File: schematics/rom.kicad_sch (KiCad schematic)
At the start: 8 parts, among them J3 XLR3_Switched, J4 XLR3_Switched, J5 myBus, U4 71256SA, U5 4NAND

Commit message: Fix errors in schematics
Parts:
- removed J3, J4: XLR3_Switched, symbol Connector:XLR3_Switched
- added SW2, SW3: SW_SPDT, symbol Switch:SW_SPDT
- renumbered J5 to J3
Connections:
- net +5V: now also SW2.3 (C), SW3.3 (C)
- net GND: now also SW2.1 (A), SW3.1 (A)
- net Prog: now also SW2.2 (B)
- net at U4.1 (A14): now also SW3.2 (B)
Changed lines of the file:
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@@
 	(wire
 		(pts
-			(xy 45.72 96.52) (xy 41.91 96.52)
+			(xy 41.91 96.52) (xy 48.26 96.52)
 		)
 		(stroke
@@
 	(wire
 		(pts
+			(xy 71.12 68.58) (xy 82.55 68.58)
+		)
+		(stroke
+			(width 0)
+			(type default)
+		)
+	)
+	(wire
+		(pts
 			(xy 82.55 96.52) (xy 77.47 96.52)
 		)
@@
 	(wire
 		(pts
+			(xy 58.42 93.98) (xy 60.96 93.98)
+		)
+		(stroke
+			(width 0)
+			(type default)
+		)
+	)
+	(wire
+		(pts
 			(xy 156.21 83.82) (xy 156.21 88.9)
 		)
@@
 	(wire
 		(pts
-			(xy 41.91 91.44) (xy 45.72 91.44)
+			(xy 41.91 91.44) (xy 48.26 91.44)
 		)
 		(stroke
@@
 	(wire
 		(pts
-			(xy 54.61 66.04) (xy 58.42 66.04)
+			(xy 54.61 66.04) (xy 60.96 66.04)
 		)
 		(stroke
@@
 	(wire
 		(pts
-			(xy 58.42 71.12) (xy 54.61 71.12)
-		)
-		(stroke
-			(width 0)
-			(type default)
-		)
-	)
-	(wire
-		(pts
-			(xy 82.55 68.58) (xy 73.66 68.58)
+			(xy 54.61 71.12) (xy 60.96 71.12)
 		)
 		(stroke
@@
 		)
 	)
+	(label "D[0..7]"
+		(at 138.43 129.54 90)
+		(fields_autoplaced yes)
+		(effects
+			(font
+				(size 1.27 1.27)
+				(bold yes)
+			)
+			(justify left bottom)
+		)
+	)
 	(label "D6"
 		(at 106.68 93.98 0)
@@
 		)
 	)
+	(label "A[0..15]"
+		(at 115.57 132.08 90)
+		(fields_autoplaced yes)
+		(effects
+			(font
+				(size 1.27 1.27)
+				(bold yes)
+			)
+			(justify left bottom)
+		)
+	)
 	(label "D0"
 		(at 120.65 142.24 90)
@@
 			)
 			(justify left bottom)
+		)
+	)
+	(symbol
+		(lib_id "Switch:SW_SPDT")
+		(at 66.04 68.58 180)
+		(unit 1)
+		(exclude_from_sim no)
+		(in_bom yes)
+		(on_board yes)
+		(dnp no)
+		(fields_autoplaced yes)
+		(property "Reference" "SW3"
+			(at 66.04 59.69 0)
+			(effects
+				(font
+					(size 1.27 1.27)
+				)
+			)
+		)
+		(property "Value" "SW_SPDT"
+			(at 66.04 62.23 0)
+			(effects
+				(font
+					(size 1.27 1.27)
+				)
+			)
+		)
+		(property "Footprint" ""
+			(at 66.04 68.58 0)
+			(effects
+				(font
+					(size 1.27 1.27)
+				)
+				(hide yes)
+			)
+		)
+		(property "Datasheet" "~"
+			(at 66.04 60.96 0)
+			(effects
+				(font
+					(size 1.27 1.27)
+				)
+				(hide yes)
+			)
+		)
+		(property "Description" "Switch, single pole double throw"
+			(at 66.04 68.58 0)
+			(effects
+				(font
+					(size 1.27 1.27)
+				)
+				(hide yes)
+			)
+		)
+		(pin "1"
+		)
+		(pin "3"
+		)
+		(pin "2"
+		)
+		(instances
+			(project "markus"
+				(path "/03a78ca6-eaff-4f05-be7b-36cd15f8b56d/4e0565c2-54d5-42cd-9fad-4b6deda009d9"
+					(reference "SW3")
+					(unit 1)
+				)
+			)
 		)
 	)
@@
 	)
 	(symbol
+		(lib_id "Switch:SW_SPDT")
+		(at 53.34 93.98 180)
+		(unit 1)
+		(exclude_from_sim no)
+		(in_bom yes)
+		(on_board yes)
+		(dnp no)
+		(fields_autoplaced yes)
+		(property "Reference" "SW2"
+			(at 53.34 85.09 0)
+			(effects
+				(font
+					(size 1.27 1.27)
+				)
+			)
+		)
+		(property "Value" "SW_SPDT"
+			(at 53.34 87.63 0)
+			(effects
+				(font
+					(size 1.27 1.27)
+				)
+			)
+		)
+		(property "Footprint" ""
+			(at 53.34 93.98 0)
+			(effects
+				(font
+					(size 1.27 1.27)
+				)
+				(hide yes)
+			)
+		)
+		(property "Datasheet" "~"
+			(at 53.34 86.36 0)
+			(effects
+				(font
+					(size 1.27 1.27)
+				)
+				(hide yes)
+			)
+		)
+		(property "Description" "Switch, single pole double throw"
+			(at 53.34 93.98 0)
+			(effects
+				(font
+					(size 1.27 1.27)
+				)
+				(hide yes)
+			)
+		)
+		(pin "1"
+		)
+		(pin "3"
+		)
+		(pin "2"
+		)
+		(instances
+			(project ""
+				(path "/03a78ca6-eaff-4f05-be7b-36cd15f8b56d/4e0565c2-54d5-42cd-9fad-4b6deda009d9"
+					(reference "SW2")
+					(unit 1)
+				)
+			)
+		)
+	)
+	(symbol
 		(lib_id "power:+5V")
 		(at 48.26 135.89 0)
@@
 	)
 	(symbol
-		(lib_id "Connector:XLR3_Switched")
-		(at 66.04 68.58 180)
-		(unit 2)
-		(exclude_from_sim no)
-		(in_bom yes)
-		(on_board yes)
-		(dnp no)
-		(property "Reference" "J4"
-			(at 66.04 59.2582 0)
-			(effects
-				(font
-					(size 1.27 1.27)
-				)
-			)
-		)
-		(property "Value" "XLR3_Switched"
-			(at 66.04 61.5696 0)
-			(effects
-				(font
-					(size 1.27 1.27)
-				)
-			)
-		)
-		(property "Footprint" ""
-			(at 66.04 71.12 0)
-			(effects
-				(font
-					(size 1.27 1.27)
-				)
-				(hide yes)
-			)
-		)
-		(property "Datasheet" " ~"
-			(at 66.04 71.12 0)
-			(effects
-				(font
-					(size 1.27 1.27)
-				)
-				(hide yes)
-			)
-		)
-		(property "Description" ""
-			(at 66.04 68.58 0)
-			(effects
-				(font
-					(size 1.27 1.27)
-				)
-				(hide yes)
-			)
-		)
-		(pin "3"
-		)
-		(pin "1"
-		)
-		(pin "2"
-		)
-		(pin "NO"
-		)
-		(pin "N"
-		)
-		(pin "NC"
-		)
-		(instances
-			(project "markus"
-				(path "/03a78ca6-eaff-4f05-be7b-36cd15f8b56d/4e0565c2-54d5-42cd-9fad-4b6deda009d9"
-					(reference "J4")
-					(unit 2)
-				)
-			)
-		)
-	)
-	(symbol
-		(lib_id "Connector:XLR3_Switched")
-		(at 53.34 93.98 180)
-		(unit 2)
-		(exclude_from_sim no)
-		(in_bom yes)
-		(on_board yes)
-		(dnp no)
-		(property "Reference" "J3"
-			(at 53.34 84.6582 0)
-			(effects
-				(font
-					(size 1.27 1.27)
-				)
-			)
-		)
-		(property "Value" "XLR3_Switched"
-			(at 53.34 86.9696 0)
-			(effects
-				(font
-					(size 1.27 1.27)
-				)
-			)
-		)
-		(property "Footprint" ""
-			(at 53.34 96.52 0)
-			(effects
-				(font
-					(size 1.27 1.27)
-				)
-				(hide yes)
-			)
-		)
-		(property "Datasheet" " ~"
-			(at 53.34 96.52 0)
-			(effects
-				(font
-					(size 1.27 1.27)
-				)
-				(hide yes)
-			)
-		)
-		(property "Description" ""
-			(at 53.34 93.98 0)
-			(effects
-				(font
-					(size 1.27 1.27)
-				)
-				(hide yes)
-			)
-		)
-		(pin "2"
-		)
-		(pin "NO"
-		)
-		(pin "3"
-		)
-		(pin "1"
-		)
-		(pin "NC"
-		)
-		(pin "N"
-		)
-		(instances
-			(project "markus"
-				(path "/03a78ca6-eaff-4f05-be7b-36cd15f8b56d/4e0565c2-54d5-42cd-9fad-4b6deda009d9"
-					(reference "J3")
-					(unit 2)
-				)
-			)
-		)
-	)
-	(symbol
 		(lib_id "6502:myBus")
 		(at 99.06 151.13 0)
@@
 		(on_board yes)
 		(dnp no)
-		(property "Reference" "J5"
+		(property "Reference" "J3"
 			(at 104.775 158.0642 0)
 			(effects
@@
 			(project "markus"
 				(path "/03a78ca6-eaff-4f05-be7b-36cd15f8b56d/4e0565c2-54d5-42cd-9fad-4b6deda009d9"
-					(reference "J5")
+					(reference "J3")
 					(unit 1)
 				)

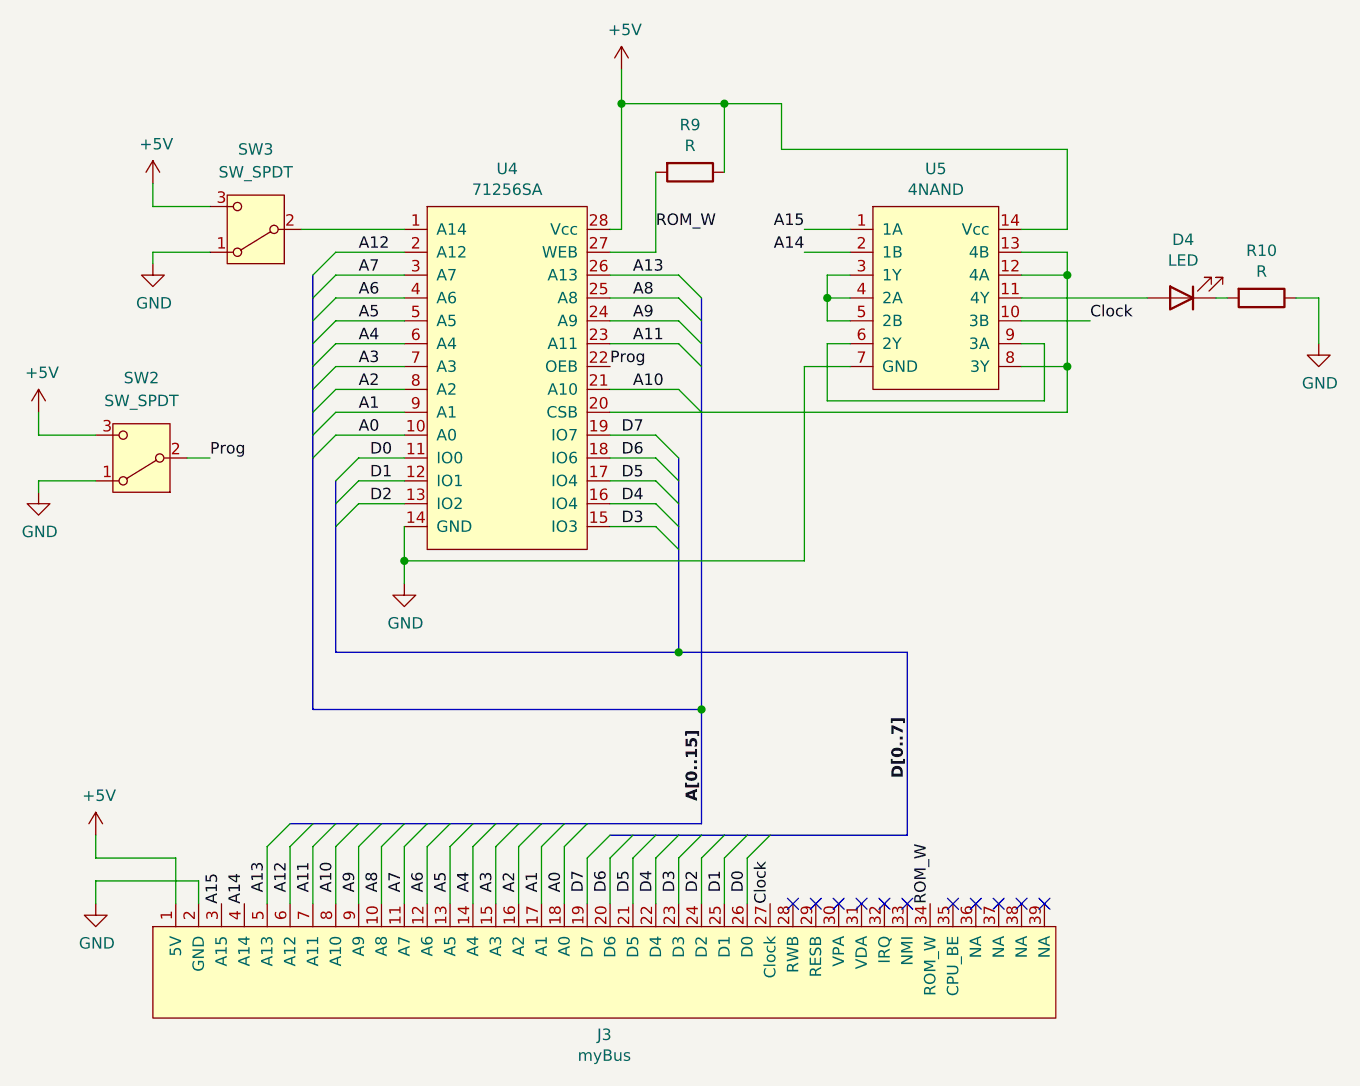
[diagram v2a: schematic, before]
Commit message: Update ROM design
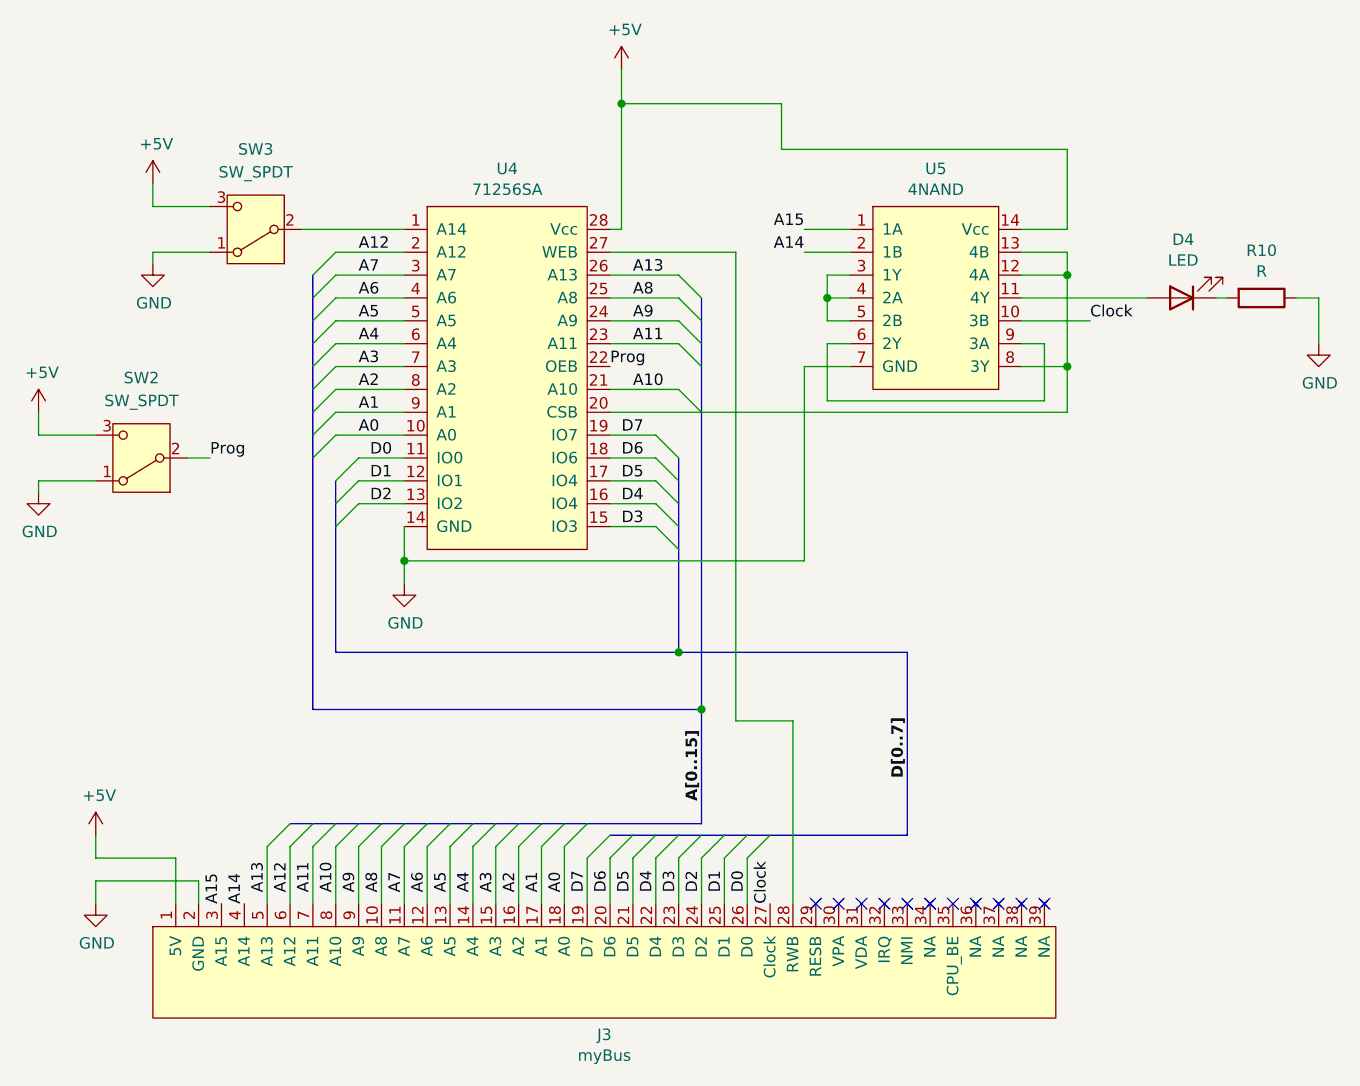
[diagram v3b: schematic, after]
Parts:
- removed R9: R, symbol Device:R
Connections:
- net at J3.28 (RWB): now also U4.27 (WEB)
- net ROM_W: no longer names the net of J3.34 (NA)
- net ROM_W: no longer U4.27 (WEB)
